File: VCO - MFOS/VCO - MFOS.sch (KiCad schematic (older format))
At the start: 54 parts, among them J1 CV1, J12 RV1P2, J13 RV2P2, J14 RV1P1, J15 RV2P1, J16 RV2P3, J17 RV1P3, J2 CV2, J3 CV3, J4 CV4, J5 LIN, J6 SYNC, Q1 SSM2210, Q2 Q_PJFET_GSD, U1 OP275, U2 TL072

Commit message: whoops
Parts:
- removed Q2: Q_PJFET_GSD, Package_TO_SOT_THT:TO-92, symbol Device:Q_PJFET_GSD
- added Q2: Q_PJFET_DSG, Package_TO_SOT_THT:TO-92L_Inline_Wide, symbol Device:Q_PJFET_DSG
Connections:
- net Earth: now also Q1.2 (B1); no longer Q1.7 (B2)
- net RAW: now also Q2.2 (S)
- net at C2.1, R14.1, R17.2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: now also Q1.8 (C2); no longer Q1.1 (C1)
- net at C3.1, U2.2 (-): now also Q1.1 (C1), Q2.1 (D); no longer Q1.8 (C2)
- net at D1.2 (A), RV3.2: now also Q1.7 (B2); no longer Q1.2 (B1)
- net at R18.2: now also Q2.3 (G)
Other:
- moved on the sheet: Q1A, Q1B
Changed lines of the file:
@@
-$EndComp
-$Comp
-L Device:Q_PJFET_GSD Q2
-U 1 1 5F963F8C
-P 6950 5700
-F 0 "Q2" V 7278 5700 50  0000 C CNN
-F 1 "Q_PJFET_GSD" V 7187 5700 50  0000 C CNN
-F 2 "Package_TO_SOT_THT:TO-92" H 7150 5800 50  0001 C CNN
-F 3 "~" H 6950 5700 50  0001 C CNN
-	1    6950 5700
-	0    -1   -1   0
 $EndComp
 $Comp
@@
 L Transistor_BJT:SSM2210 Q1
 U 2 1 5F99D44C
+P 4350 2700
+F 0 "Q1" H 4541 2654 50  0000 L CNN
+F 1 "SSM2210" H 4541 2745 50  0000 L CNN
+F 2 "Package_DIP:DIP-8_W7.62mm_Socket" H 4350 2700 50  0001 C CNN
+F 3 "https://www.analog.com/media/en/technical-documentation/obsolete-data-sheets/SSM2210.pdf" H 4350 2700 50  0001 C CNN
+	2    4350 2700
+	1    0    0    1
+$EndComp
+$Comp
+L Transistor_BJT:SSM2210 Q1
+U 1 1 5F9A02FE
 P 5050 2700
 F 0 "Q1" H 5241 2654 50  0000 L CNN
@@
 F 2 "Package_DIP:DIP-8_W7.62mm_Socket" H 5050 2700 50  0001 C CNN
 F 3 "https://www.analog.com/media/en/technical-documentation/obsolete-data-sheets/SSM2210.pdf" H 5050 2700 50  0001 C CNN
-	2    5050 2700
-	-1   0    0    1
-$EndComp
-$Comp
-L Transistor_BJT:SSM2210 Q1
-U 1 1 5F9A02FE
-P 4350 2700
-F 0 "Q1" H 4541 2654 50  0000 L CNN
-F 1 "SSM2210" H 4541 2745 50  0000 L CNN
-F 2 "Package_DIP:DIP-8_W7.62mm_Socket" H 4350 2700 50  0001 C CNN
-F 3 "https://www.analog.com/media/en/technical-documentation/obsolete-data-sheets/SSM2210.pdf" H 4350 2700 50  0001 C CNN
-	1    4350 2700
-	1    0    0    1
+	1    5050 2700
+	-1   0    0    1
 $EndComp
 Wire Wire Line
@@
 Wire Wire Line
 	7750 3400 7750 3500
+$Comp
+L Device:Q_PJFET_DSG Q2
+U 1 1 5FDC50C1
+P 6950 5700
+F 0 "Q2" V 7278 5700 50  0000 C CNN
+F 1 "Q_PJFET_DSG" V 7187 5700 50  0000 C CNN
+F 2 "Package_TO_SOT_THT:TO-92L_Inline_Wide" H 7150 5800 50  0001 C CNN
+F 3 "~" H 6950 5700 50  0001 C CNN
+	1    6950 5700
+	0    -1   -1   0
+$EndComp
 $EndSCHEMATC

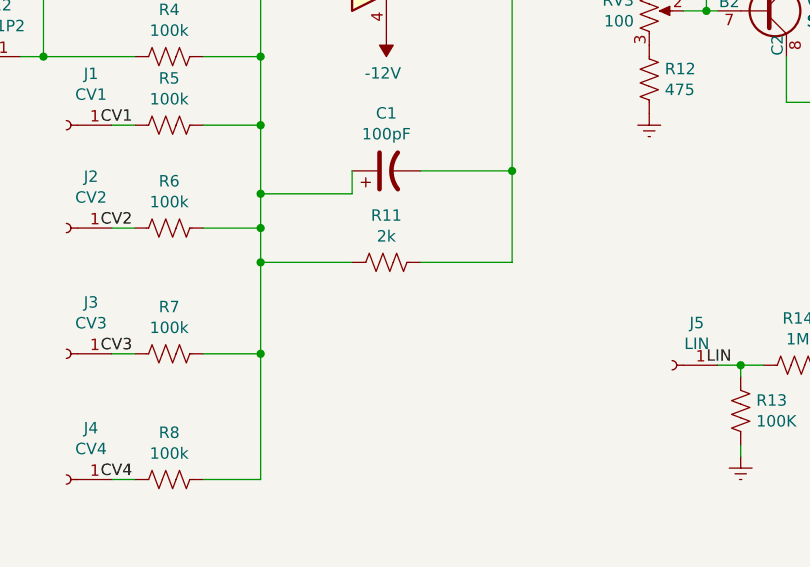
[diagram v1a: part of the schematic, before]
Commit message: VCO - added tempco resistor holes
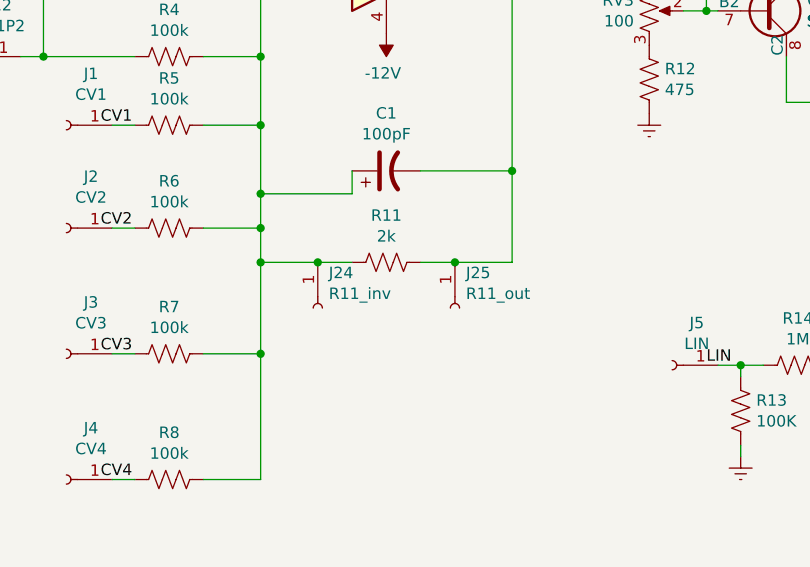
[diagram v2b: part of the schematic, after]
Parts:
- added J24: R11_inv, Connector_Wire:SolderWirePad_1x01_Drill1mm, symbol Connector:Conn_01x01_Female
- added J25: R11_out, Connector_Wire:SolderWirePad_1x01_Drill1mm, symbol Connector:Conn_01x01_Female
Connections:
- net at C1.1, R11.2, R3.1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: now also J24.1 (Pin_1)
- net at C1.2, R11.1, RV3.1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: now also J25.1 (Pin_1)
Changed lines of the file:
@@
 Connection ~ 2150 3800
 Wire Wire Line
-	2150 3800 2550 3800
+	2150 3800 2400 3800
 Wire Wire Line
 	2150 3500 2550 3500
@@
 	2550 3500 2550 3400
 Wire Wire Line
-	2850 3800 3250 3800
+	2850 3800 3000 3800
 Wire Wire Line
 	3250 3800 3250 3400
@@
 	0    -1   -1   0
 $EndComp
+$Comp
+L Connector:Conn_01x01_Female J24
+U 1 1 62012E0D
+P 2400 4000
+F 0 "J24" V 2246 4048 50  0000 L CNN
+F 1 "R11_inv" V 2337 4048 50  0000 L CNN
+F 2 "Connector_Wire:SolderWirePad_1x01_Drill1mm" H 2400 4000 50  0001 C CNN
+F 3 "~" H 2400 4000 50  0001 C CNN
+	1    2400 4000
+	0    1    1    0
+$EndComp
+Connection ~ 2400 3800
+Wire Wire Line
+	2400 3800 2550 3800
+$Comp
+L Connector:Conn_01x01_Female J25
+U 1 1 62013AE0
+P 3000 4000
+F 0 "J25" V 2846 4048 50  0000 L CNN
+F 1 "R11_out" V 2937 4048 50  0000 L CNN
+F 2 "Connector_Wire:SolderWirePad_1x01_Drill1mm" H 3000 4000 50  0001 C CNN
+F 3 "~" H 3000 4000 50  0001 C CNN
+	1    3000 4000
+	0    1    1    0
+$EndComp
+Connection ~ 3000 3800
+Wire Wire Line
+	3000 3800 3250 3800
 $EndSCHEMATC

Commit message: literally so much stuff
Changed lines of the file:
@@
 P 1500 850
 F 0 "J15" V 1438 762 50  0000 R CNN
-F 1 "RV2P1" V 1347 762 50  0000 R CNN
+F 1 "RV2P1" V 1600 1050 50  0000 R CNN
 F 2 "Connector_Wire:SolderWirePad_1x01_Drill1mm" H 1500 850 50  0001 C CNN
 F 3 "~" H 1500 850 50  0001 C CNN
@@
 P 2100 850
 F 0 "J16" V 2038 762 50  0000 R CNN
-F 1 "RV2P3" V 1947 762 50  0000 R CNN
+F 1 "RV2P3" V 2200 950 50  0000 R CNN
 F 2 "Connector_Wire:SolderWirePad_1x01_Drill1mm" H 2100 850 50  0001 C CNN
 F 3 "~" H 2100 850 50  0001 C CNN
@@
 P 1450 1400
 F 0 "J14" V 1388 1312 50  0000 R CNN
-F 1 "RV1P1" V 1297 1312 50  0000 R CNN
+F 1 "RV1P1" V 1500 1600 50  0000 R CNN
 F 2 "Connector_Wire:SolderWirePad_1x01_Drill1mm" H 1450 1400 50  0001 C CNN
 F 3 "~" H 1450 1400 50  0001 C CNN
@@
 P 2100 1400
 F 0 "J17" V 2038 1312 50  0000 R CNN
-F 1 "RV1P3" V 1947 1312 50  0000 R CNN
+F 1 "RV1P3" V 2150 1450 50  0000 R CNN
 F 2 "Connector_Wire:SolderWirePad_1x01_Drill1mm" H 2100 1400 50  0001 C CNN
 F 3 "~" H 2100 1400 50  0001 C CNN
